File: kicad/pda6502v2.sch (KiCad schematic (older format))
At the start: 76 parts, among them J1 GPIO1, J2 GPIO2, J3 UART, J4 Screw_Terminal_01x02, J5 Conn_02x04_Odd_Even, J6 ICSP, SW1 SW_Push, U1 W65C02SxP, U10 LT3030, U11 SC28L92A1B, U2 W65C22SxP, U3 W65C22SxP, U4 DS1818, U5 AS6C4008-55PCN, U6 AS6C4008-55PCN, U7 AT25M01, U8 ICE40HX4K-TQ144, U9 TLV1117-33, X1 8 MHz, X2 3.6864 MHz

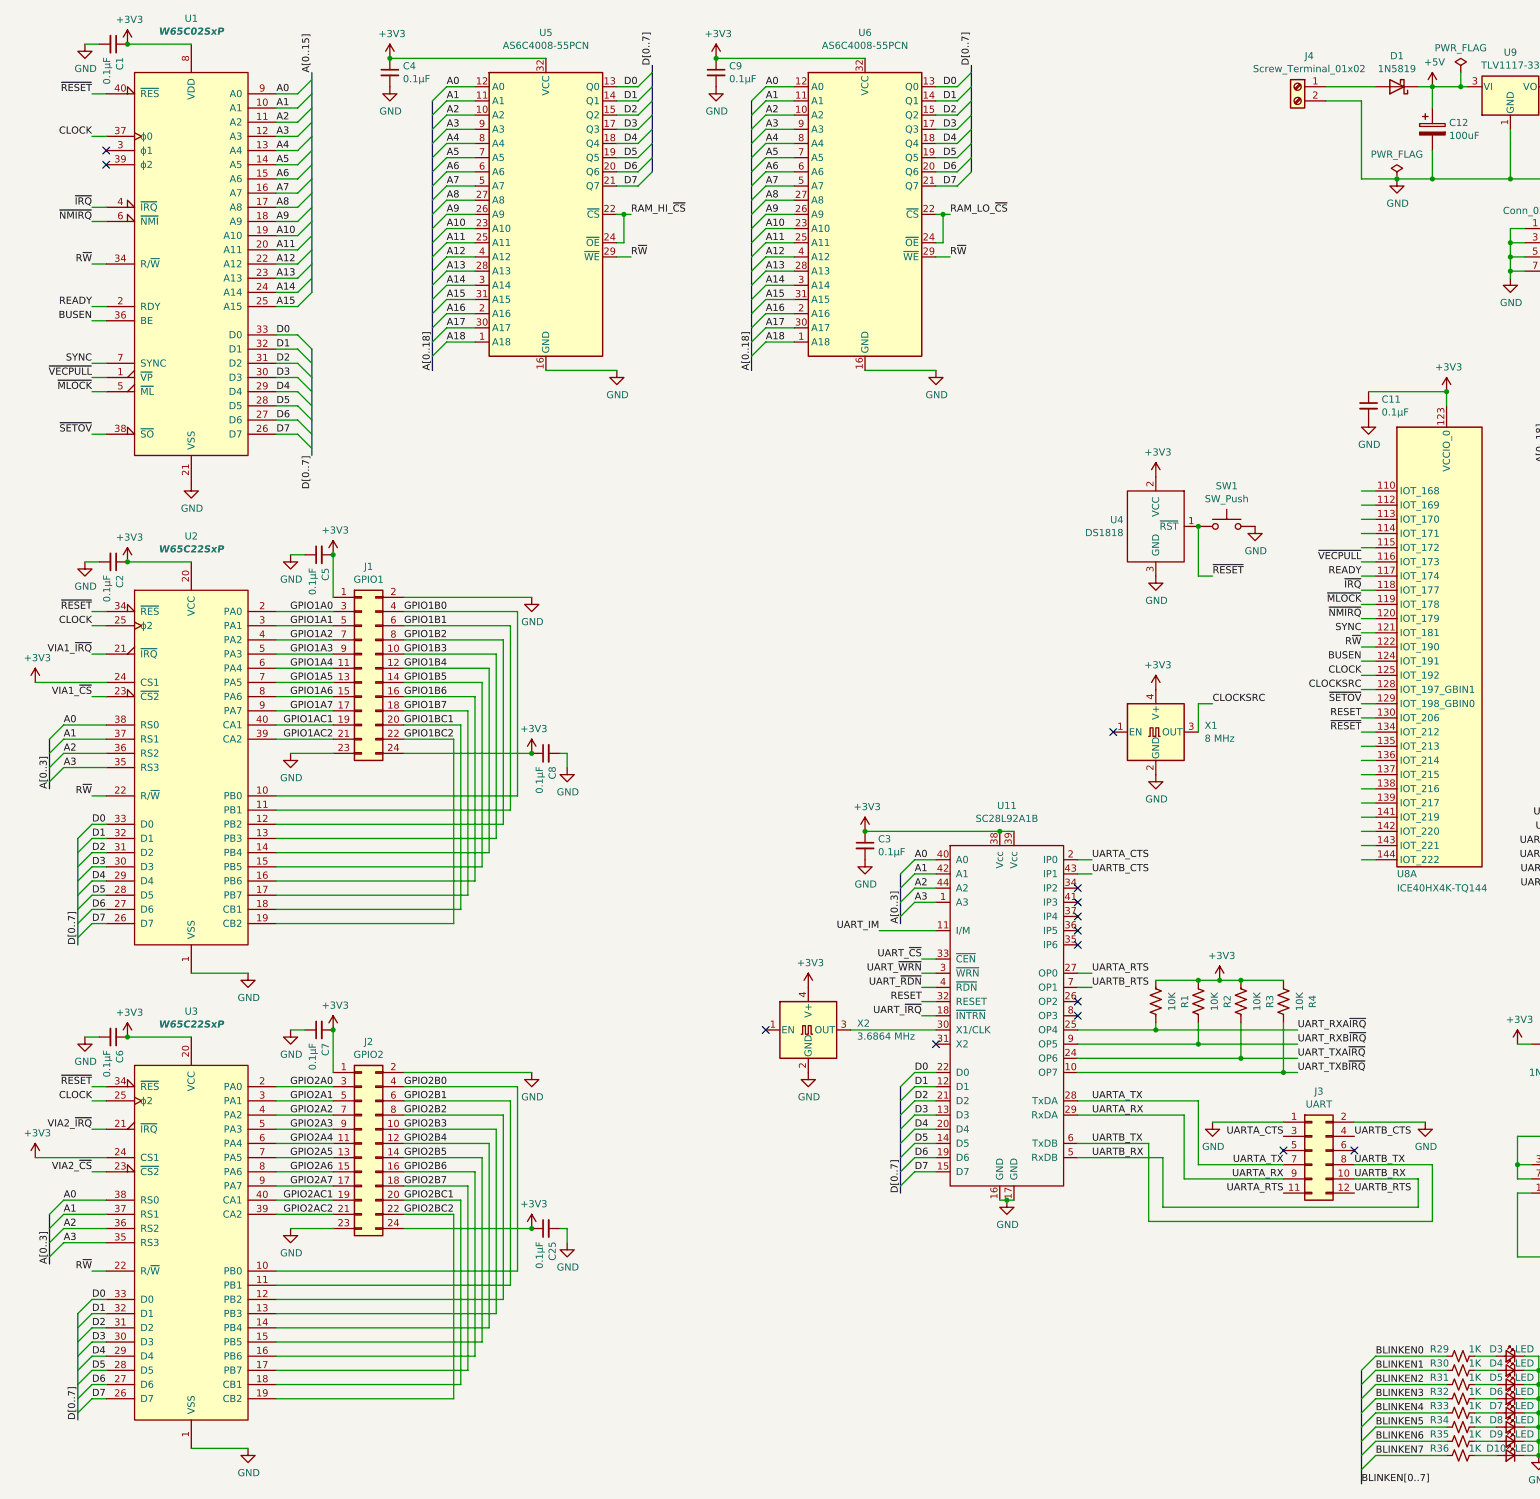
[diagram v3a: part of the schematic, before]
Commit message: Headers for SPI and EXT (FPGA expansion)
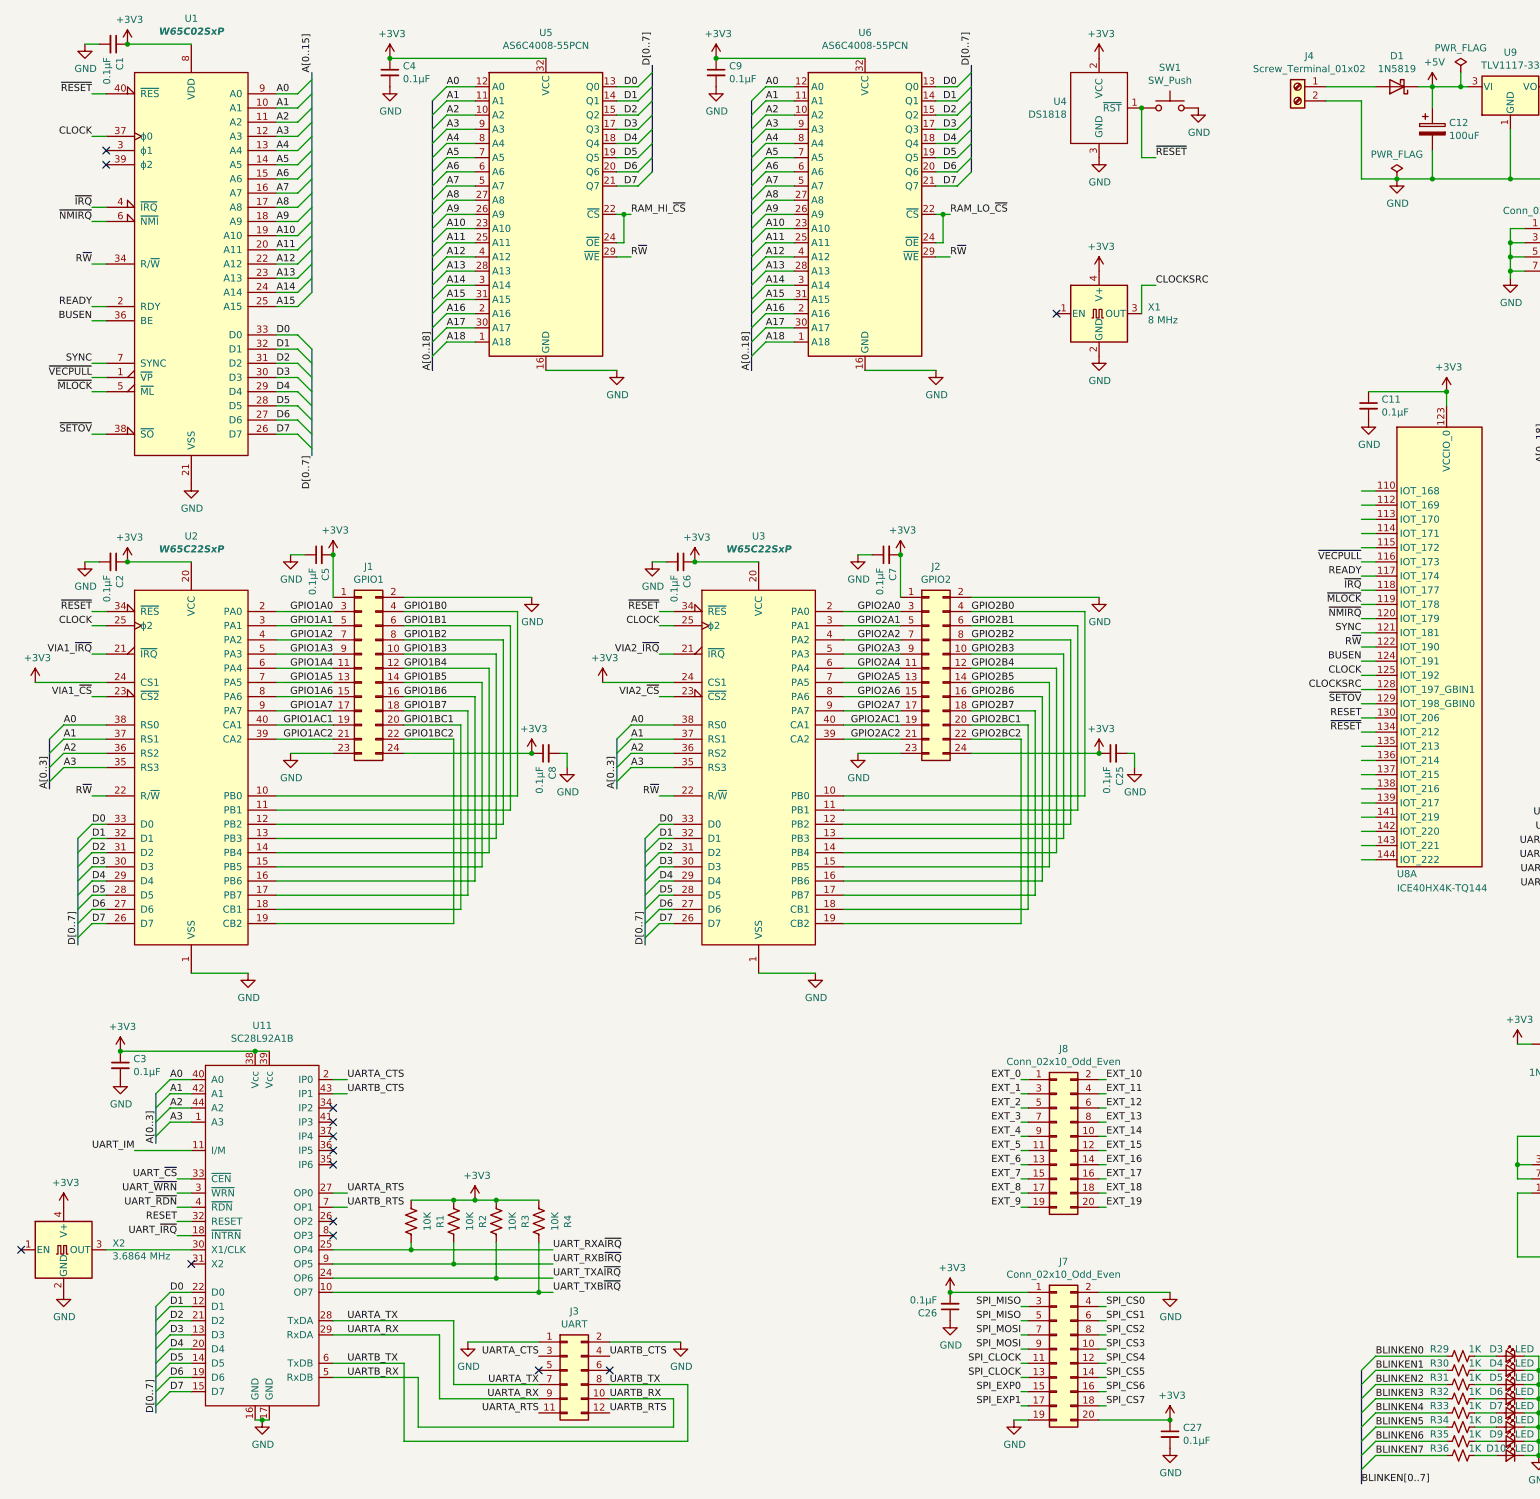
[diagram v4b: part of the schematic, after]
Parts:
- added C26, C27: 0.1μF, Capacitor_SMD:C_0805_2012Metric_Pad1.18x1.45mm_HandSolder, symbol Device:C_Small
- added J7, J8: Conn_02x10_Odd_Even, Connector_PinHeader_2.54mm:PinHeader_2x10_P2.54mm_Vertical, symbol Connector_Generic:Conn_02x10_Odd_Even
- J1, J2: footprint Connector_PinSocket_2.54mm:PinSocket_2x12_P2.54mm_Vertical -> Connector_PinHeader_2.54mm:PinHeader_2x12_P2.54mm_Vertical
- J5: footprint Connector_PinSocket_2.54mm:PinSocket_2x04_P2.54mm_Vertical -> Connector_PinHeader_2.54mm:PinHeader_2x04_P2.54mm_Vertical
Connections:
- net +3V3: now also C26.2, C27.1, J7.1 (Pin_1), J7.20 (Pin_20)
- net GND: now also C26.1, C27.2, J7.19 (Pin_19), J7.2 (Pin_2)
- new net EXT_0: J8.1 (Pin_1)
- new net EXT_1: J8.3 (Pin_3)
- new net EXT_10: J8.2 (Pin_2)
- new net EXT_11: J8.4 (Pin_4)
- new net EXT_12: J8.6 (Pin_6)
- new net EXT_13: J8.8 (Pin_8)
- new net EXT_14: J8.10 (Pin_10)
- new net EXT_15: J8.12 (Pin_12)
- new net EXT_16: J8.14 (Pin_14)
- new net EXT_17: J8.16 (Pin_16)
- new net EXT_18: J8.18 (Pin_18)
- new net EXT_19: J8.20 (Pin_20)
- new net EXT_2: J8.5 (Pin_5)
- new net EXT_3: J8.7 (Pin_7)
- new net EXT_4: J8.9 (Pin_9)
- new net EXT_5: J8.11 (Pin_11)
- new net EXT_6: J8.13 (Pin_13)
- new net EXT_7: J8.15 (Pin_15)
- new net EXT_8: J8.17 (Pin_17)
- new net EXT_9: J8.19 (Pin_19)
- new net SPI_CLOCK: J7.11 (Pin_11), J7.13 (Pin_13)
- new net SPI_CS0: J7.4 (Pin_4)
- new net SPI_CS1: J7.6 (Pin_6)
- new net SPI_CS2: J7.8 (Pin_8)
- new net SPI_CS3: J7.10 (Pin_10)
- new net SPI_CS4: J7.12 (Pin_12)
- new net SPI_CS5: J7.14 (Pin_14)
- new net SPI_CS6: J7.16 (Pin_16)
- new net SPI_CS7: J7.18 (Pin_18)
- new net SPI_EXP0: J7.15 (Pin_15)
- new net SPI_EXP1: J7.17 (Pin_17)
- new net SPI_MISO: J7.3 (Pin_3), J7.5 (Pin_5)
- new net SPI_MOSI: J7.7 (Pin_7), J7.9 (Pin_9)
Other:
- moved on the sheet: C25, C3, C6, C7, J2, J3, R1, R2, R3, R4, SW1, U11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

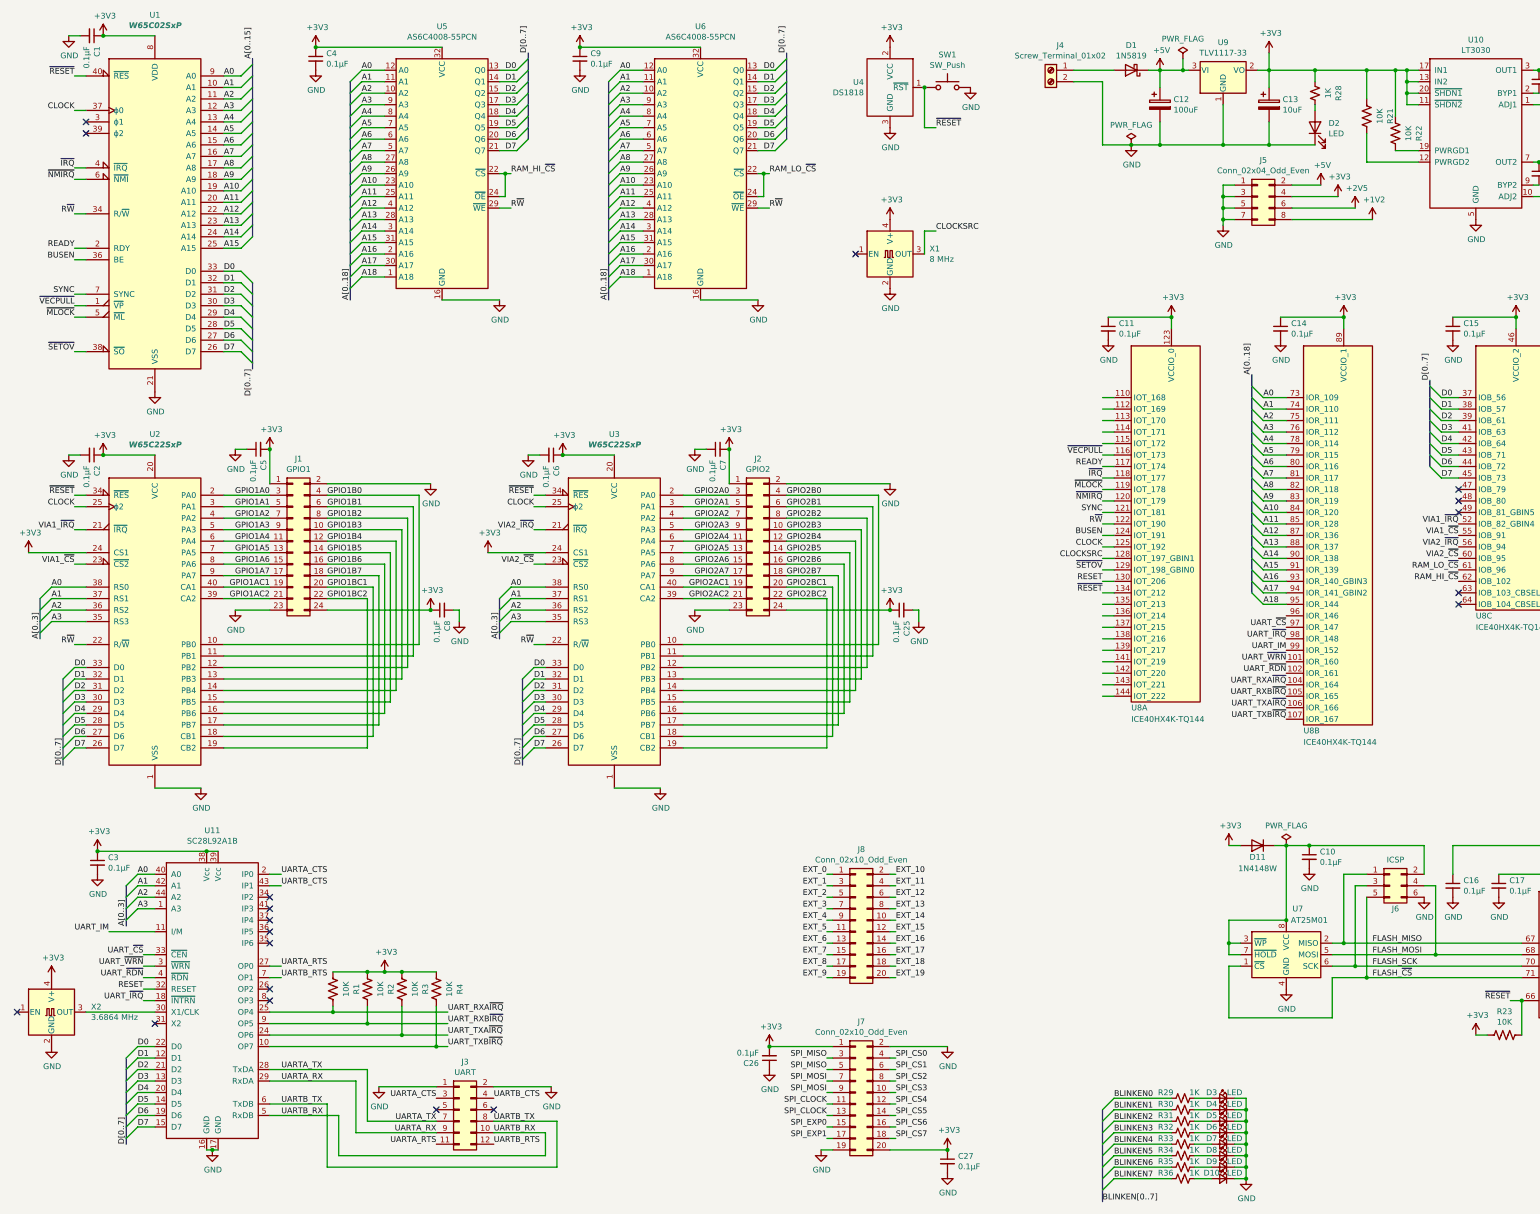
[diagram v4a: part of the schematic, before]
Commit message: ARMSID instead of second 512 KiB RAM
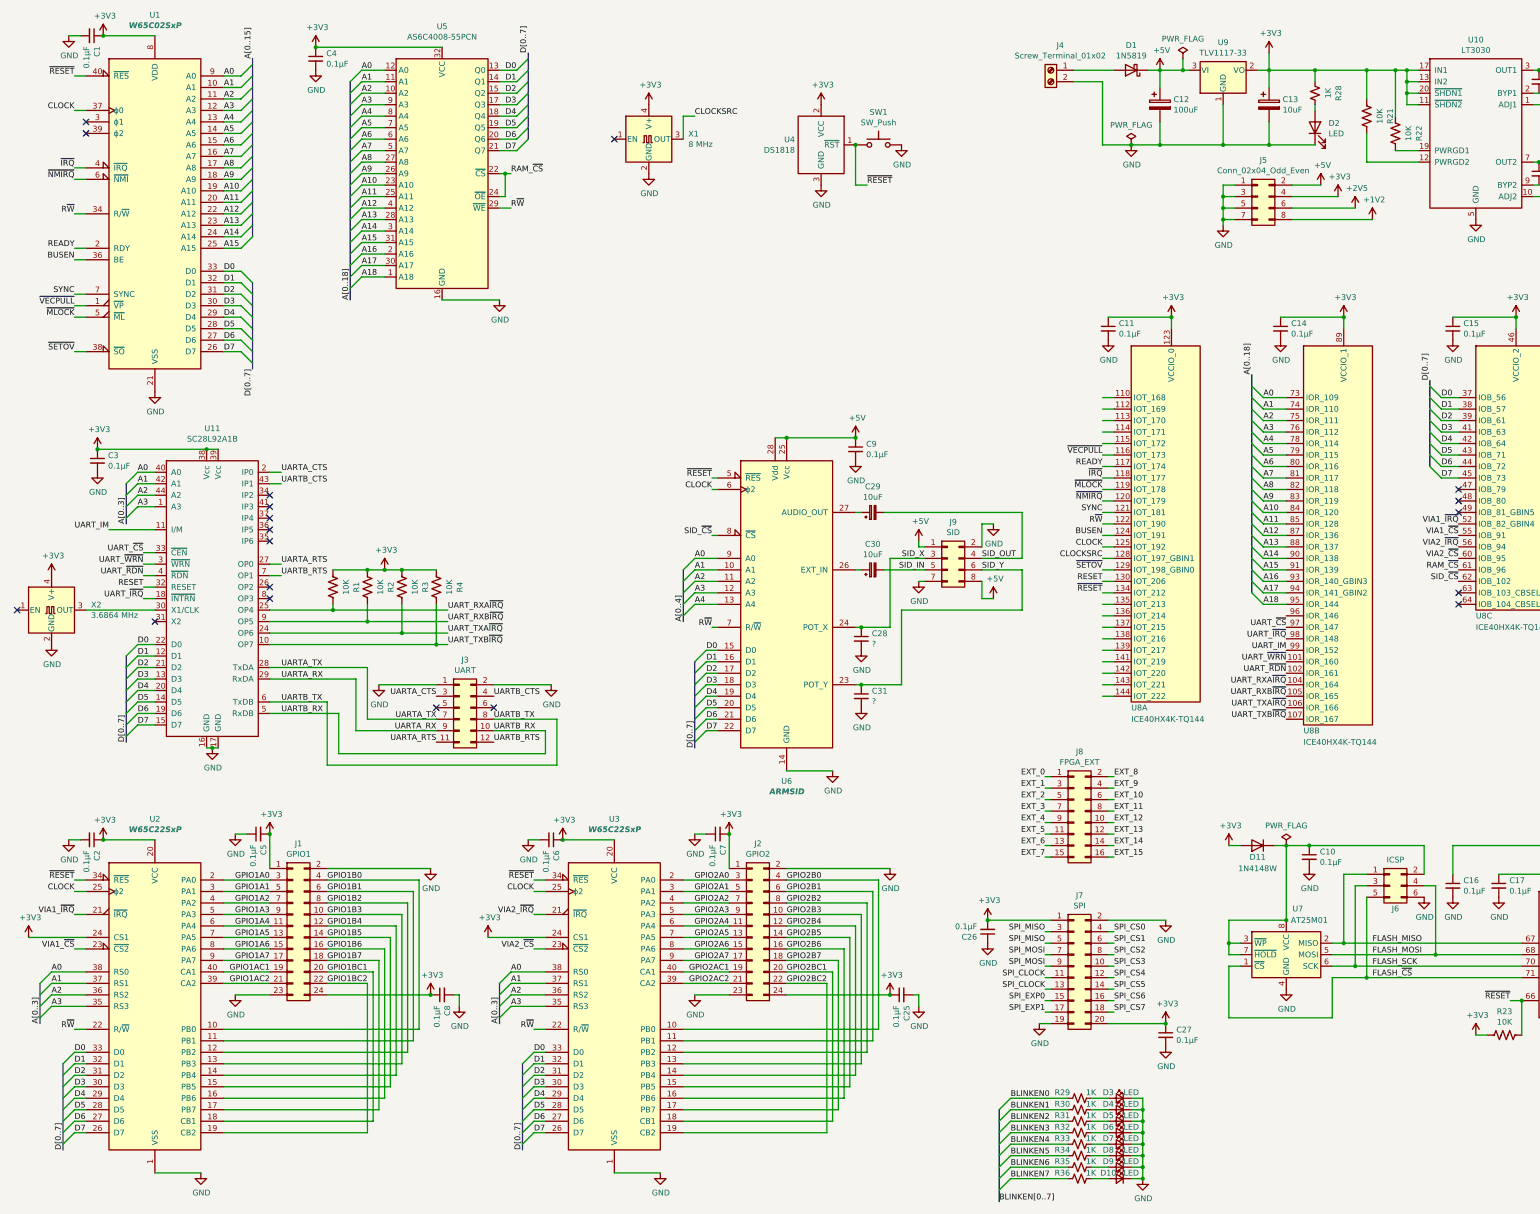
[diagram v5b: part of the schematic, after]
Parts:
- removed J8: Conn_02x10_Odd_Even, Connector_PinHeader_2.54mm:PinHeader_2x10_P2.54mm_Vertical, symbol Connector_Generic:Conn_02x10_Odd_Even
- removed U6: AS6C4008-55PCN, Package_DIP:DIP-32_W15.24mm, symbol pda6502v2:AS6C4008-55PCN
- added C28, C31: ?, Capacitor_SMD:C_0805_2012Metric_Pad1.18x1.45mm_HandSolder, symbol Device:C_Small
- added C29, C30: 10uF, Capacitor_Tantalum_SMD:CP_EIA-3528-15_AVX-H_Pad1.50x2.35mm_HandSolder, symbol Device:CP_Small
- added J8: FPGA_EXT, Connector_PinHeader_2.54mm:PinHeader_2x08_P2.54mm_Vertical, symbol Connector_Generic:Conn_02x08_Odd_Even
- added J9: SID, Connector_PinHeader_2.54mm:PinHeader_2x04_P2.54mm_Vertical, symbol Connector_Generic:Conn_02x04_Odd_Even
- added U6: ARMSID, Package_DIP:DIP-28_W15.24mm_Socket, symbol pda6502v2:ARMSID
- J7: value Conn_02x10_Odd_Even -> SPI
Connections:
- net RAM_LO_~CS is gone; now on net RAM_~CS: U8.61 (IOB_96)
- net +3V3: no longer C9.1
- net +5V: now also C9.1, J9.1 (Pin_1), J9.8 (Pin_8), U6.25 (Vcc), U6.28 (Vdd)
- net A0: now also U6.9 (A0)
- net A1: now also U6.10 (A1)
- net A2: now also U6.11 (A2)
- net A3: now also U6.12 (A3)
- net A4: now also U6.13 (A4)
- net CLOCK: now also U6.6 (ϕ2)
- net D0: now also U6.15 (D0)
- net D1: now also U6.16 (D1)
- net D2: now also U6.17 (D2)
- net D3: now also U6.18 (D3)
- net D4: now also U6.19 (D4)
- net D5: now also U6.20 (D5)
- net D6: now also U6.21 (D6)
- net D7: now also U6.22 (D7)
- net EXT_0: now also J8.1 (Pin_1)
- net EXT_1: now also J8.3 (Pin_3)
- net EXT_10: now also J8.6 (Pin_6)
- net EXT_11: now also J8.8 (Pin_8)
- net EXT_12: now also J8.10 (Pin_10)
- net EXT_13: now also J8.12 (Pin_12)
- net EXT_14: now also J8.14 (Pin_14)
- net EXT_15: now also J8.16 (Pin_16)
- net EXT_2: now also J8.5 (Pin_5)
- net EXT_3: now also J8.7 (Pin_7)
- net EXT_4: now also J8.9 (Pin_9)
- net EXT_5: now also J8.11 (Pin_11)
- net EXT_6: now also J8.13 (Pin_13)
- net EXT_7: now also J8.15 (Pin_15)
- net EXT_8: now also J8.2 (Pin_2)
- net EXT_9: now also J8.4 (Pin_4)
- net GND: now also C28.2, C31.2, J9.2 (Pin_2), J9.7 (Pin_7), U6.14 (GND)
- net R~W: now also U6.7 (R/~W)
- net ~RESET: now also U6.5 (~RES)
- net RAM_HI_~CS renamed RAM_~CS
- net RAM_~CS: no longer U8.62 (IOB_102)
- new net: C30.1, U6.26 (EXT_IN)
- new net: C29.1, U6.27 (AUDIO_OUT)
- new net SID_IN: C30.2, J9.5 (Pin_5)
- new net SID_OUT: C29.2, J9.4 (Pin_4)
- new net SID_X: C28.1, J9.3 (Pin_3), U6.24 (POT_X)
- new net SID_Y: C31.1, J9.6 (Pin_6), U6.23 (POT_Y)
- new net SID_~CS: U6.8 (~CS), U8.62 (IOB_102)
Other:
- moved on the sheet: C2, C25, C26, C27, C3, C5, C6, C7, C8, D10, D3, D4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
